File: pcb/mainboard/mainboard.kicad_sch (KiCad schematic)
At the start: 74 parts, among them J1 PWR, J2 Conn_01x03_Male, J3 USB_B, J4 UI, J5 Conn_02x03_Odd_Even, J6 RES1, Q1 BSS138, Q2 TSM3401, SW1 JTP1236, SW2 JTP1236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

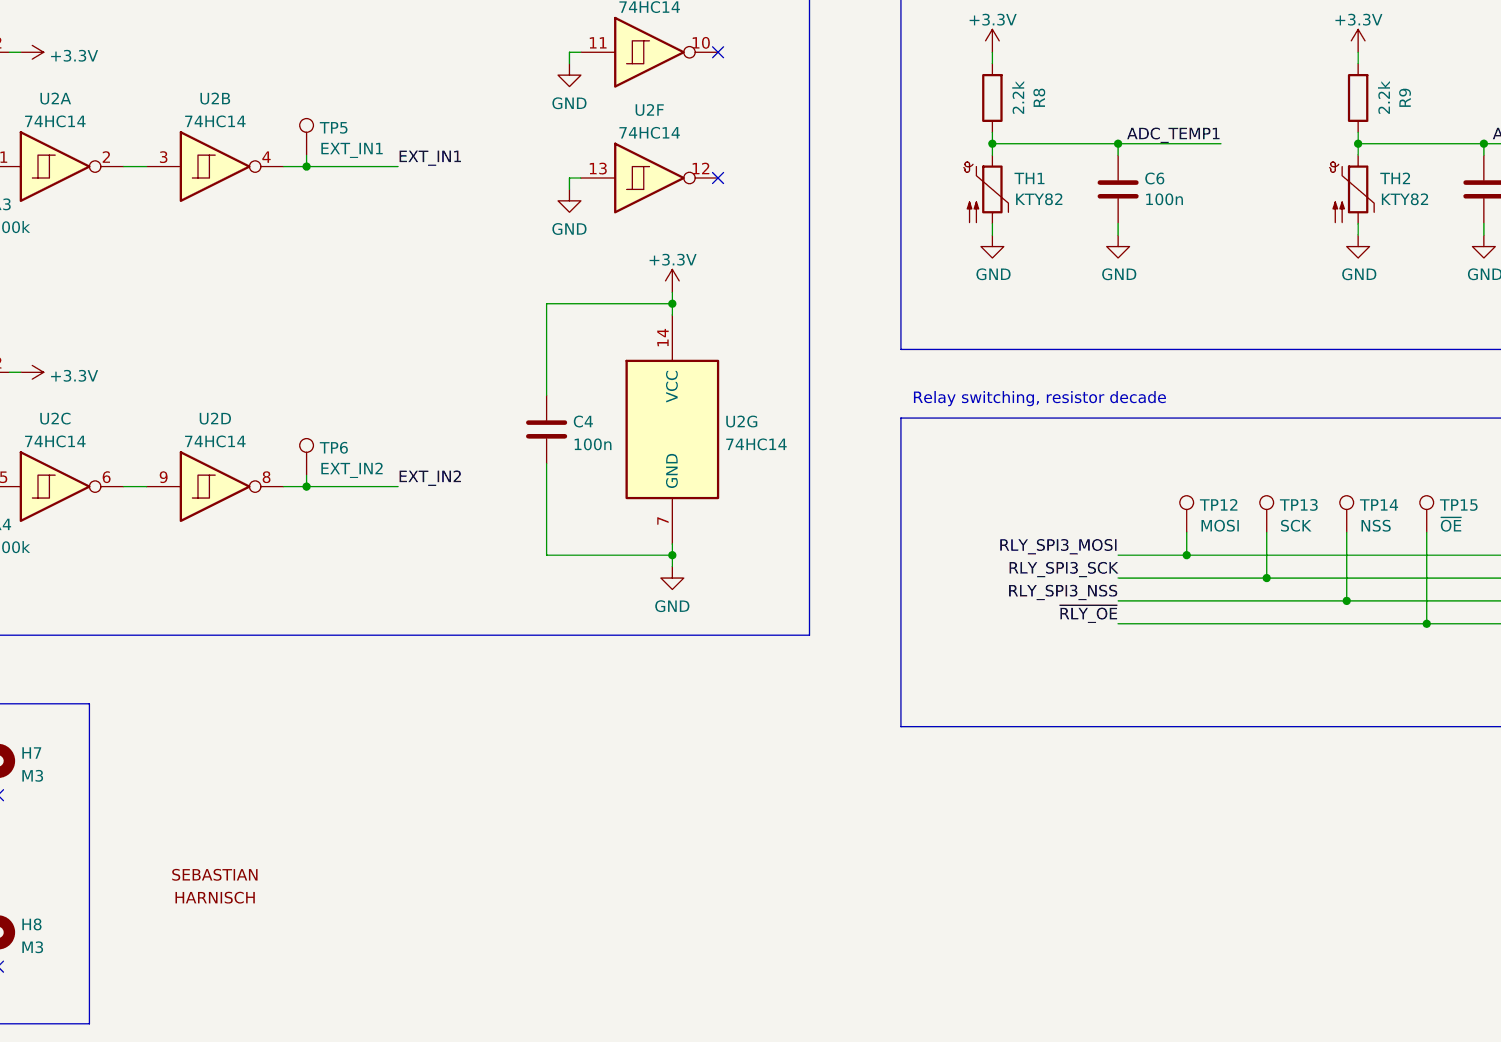
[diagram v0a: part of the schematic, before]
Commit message: Update to Kicad v9, new power supply board and other modifications
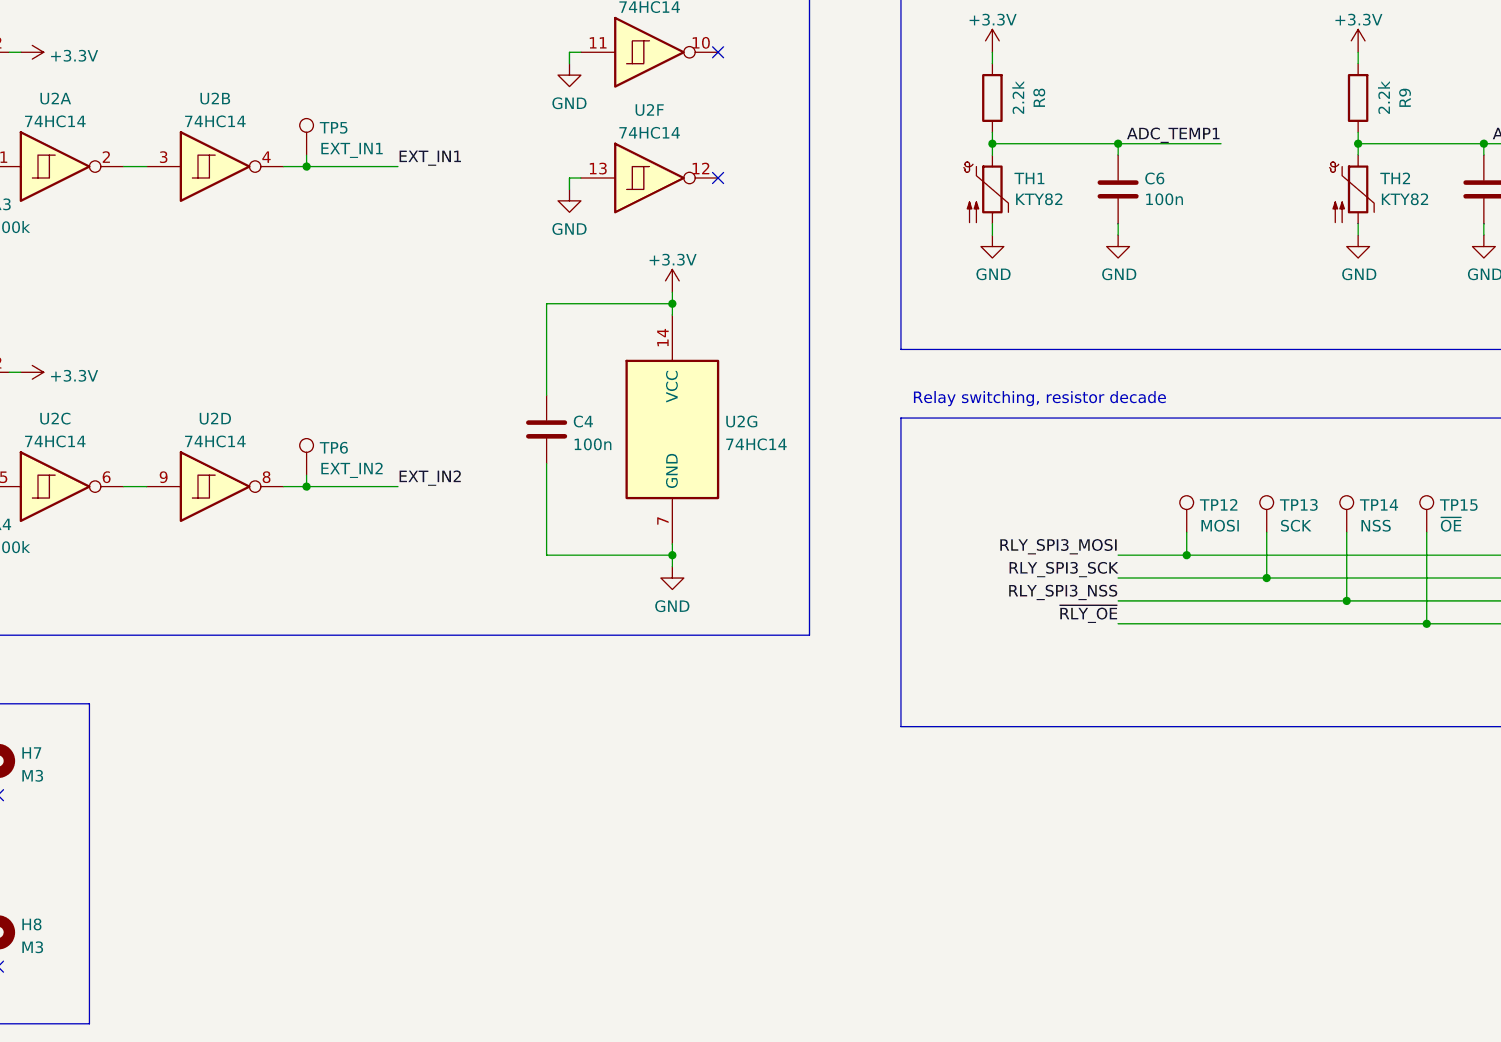
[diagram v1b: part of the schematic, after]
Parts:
- removed LOGO1: LOGO_SH, 01_Sebastian:SebastianHarnisch, symbol 01_Sebastian:LOGO_SH
